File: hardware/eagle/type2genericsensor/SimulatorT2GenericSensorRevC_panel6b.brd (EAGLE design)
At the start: 99.1 x 63.5 mm, 46 parts

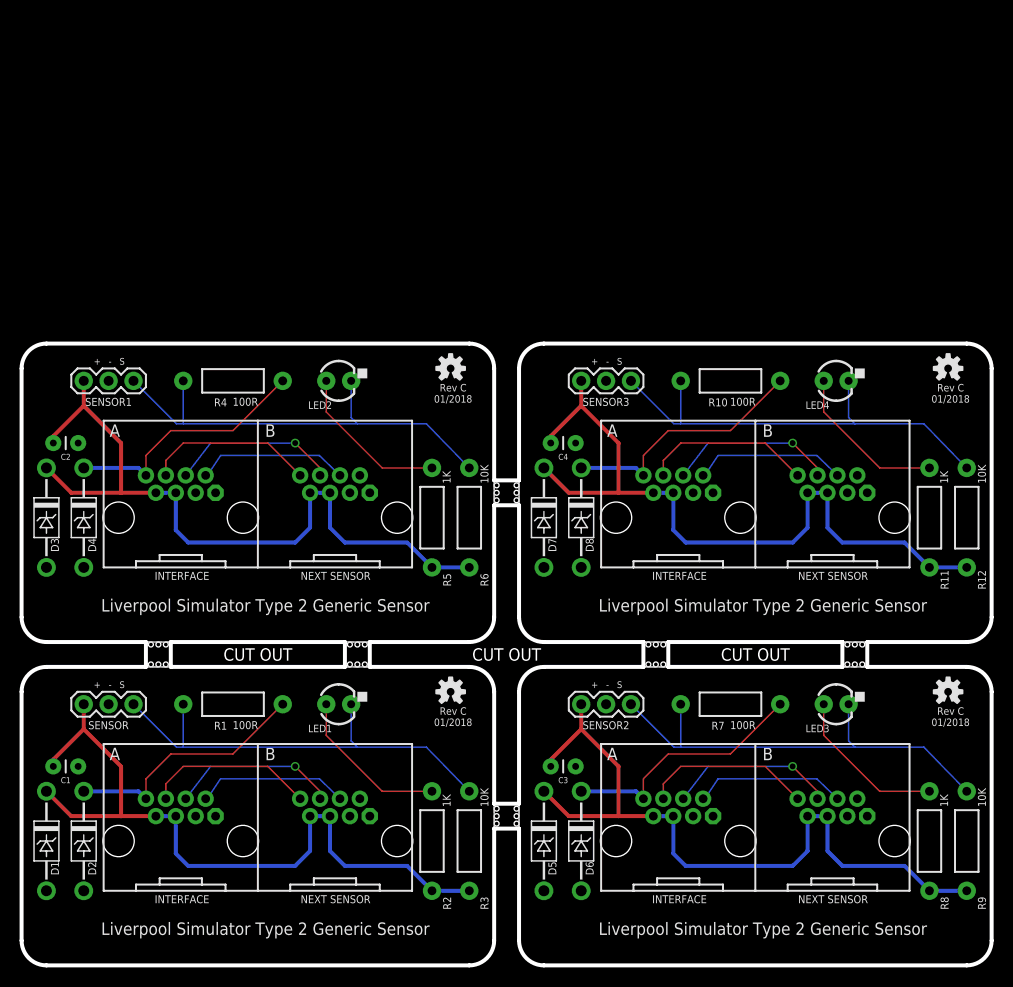
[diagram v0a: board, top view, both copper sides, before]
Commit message: Wider 5mm break-offs
Issues with JLPCB rejecting panelised boards with 2.5mm stamp hole
break-off tabs. Increased tab width to 5mm on all panelised boards.
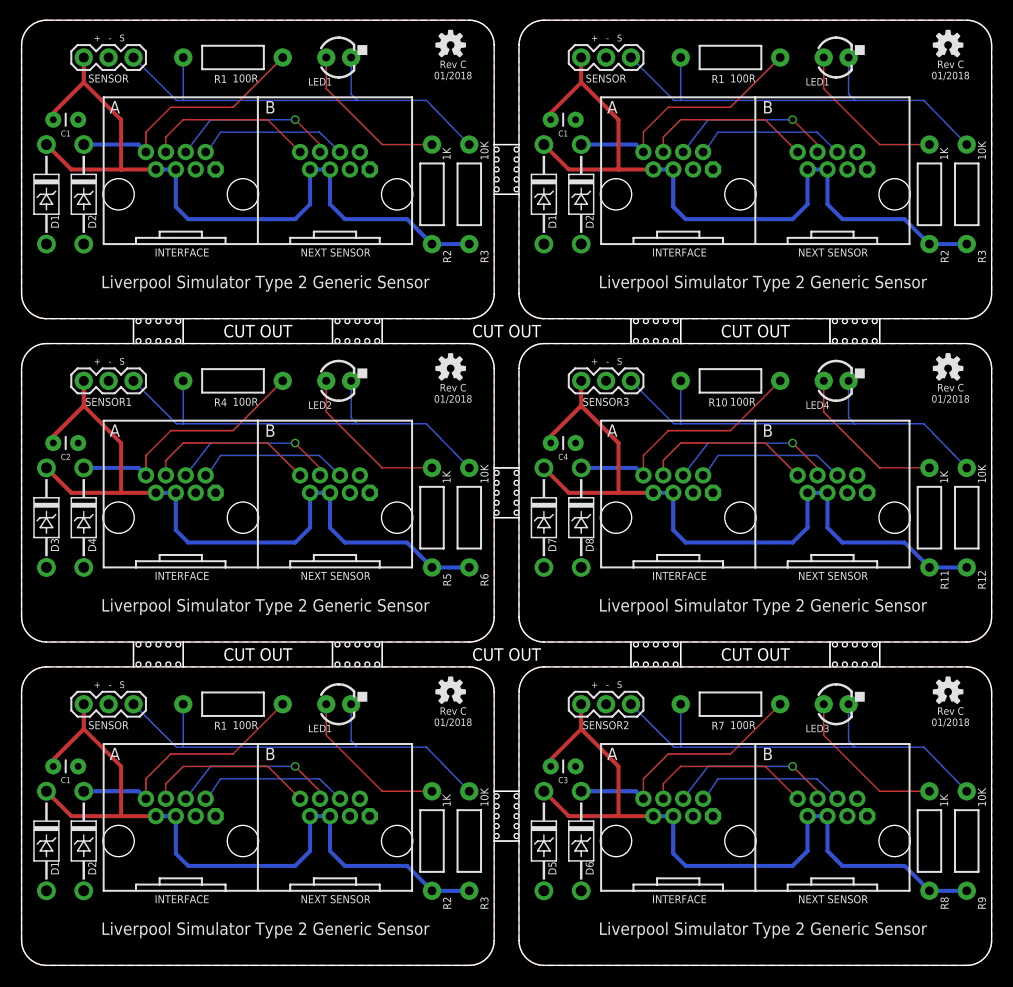
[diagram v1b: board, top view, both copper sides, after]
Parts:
- removed E$2, E$3, E$4, E$5, E$6: (no value), AIC_Custom:STAMP_HOLES
- added C1_1, C1_2: 100nF, SparkFun-Passives:CAP-PTH-SMALL
- added D1_1, D1_2, D2_1, D2_2: SA5.0A, AIC_Custom:DO41_TVS_UNI
- added JP1_1, JP1_2: RJ45-RJHSE-5080-023HOLE, AIC_Custom:RJ45-RJHSE-5080-02-3HOLE
- added LED1_1, LED1_2: Blue, SparkFun-LED:LED3MM
- added LOGO1_1, LOGO1_2: OSHW-LOGOS, SparkFun-Aesthetics:OSHW-LOGO-S
- added R1_1, R1_2: 100R, SparkFun-Passives:AXIAL-0.4
- added R2_1, R2_2: 1K, SparkFun-Passives:AXIAL-0.4
- added R3_1, R3_2: 10K, SparkFun-Passives:AXIAL-0.4
- added SENSOR_1, SENSOR_2: (no value), SparkFun-Connectors:1X03
- E$1: device AIC_Custom:STAMP_HOLES -> AIC_Custom:OUTLINE_PANEL_6_5MM
- moved E$1 46.7 mm to (0.00, 0.00)
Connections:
- new net !OUT!4: D2_1.CATHODE, JP1_1.A8, R1_1.P$1
- new net !OUT!5: D2_2.CATHODE, JP1_2.A8, R1_2.P$1
- new net B21: JP1_1.A6, JP1_1.B8
- new net B22: JP1_2.A6, JP1_2.B8
- new net B31: JP1_1.A4, JP1_1.B6
- new net B32: JP1_2.A4, JP1_2.B6
- new net B41: JP1_1.A2, JP1_1.B4
- new net B42: JP1_2.A2, JP1_2.B4
- new net GND4: C1_1.2, D1_1.ANODE, D2_1.ANODE, JP1_1.A1, JP1_1.A3, JP1_1.B1, JP1_1.B3, SENSOR_1.2
- new net GND5: C1_2.2, D1_2.ANODE, D2_2.ANODE, JP1_2.A1, JP1_2.A3, JP1_2.B1, JP1_2.B3, SENSOR_2.2
- new net LED4: LED1_1.A, R2_1.P$1
- new net LED5: LED1_2.A, R2_2.P$1
- new net SIG4: LED1_1.K, R1_1.P$2, R3_1.P$1, SENSOR_1.3
- new net SIG5: LED1_2.K, R1_2.P$2, R3_2.P$1, SENSOR_2.3
- new net VCC4: C1_1.1, D1_1.CATHODE, JP1_1.A5, JP1_1.A7, JP1_1.B5, JP1_1.B7, R2_1.P$2, R3_1.P$2, SENSOR_1.1
- new net VCC5: C1_2.1, D1_2.CATHODE, JP1_2.A5, JP1_2.A7, JP1_2.B5, JP1_2.B7, R2_2.P$2, R3_2.P$2, SENSOR_2.1
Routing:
- net VCC5: track 0.00 -> 76.1 mm
- net VCC4: track 0.00 -> 76.1 mm
- net SIG5: track 0.00 -> 47.0 mm
- net SIG4: track 0.00 -> 47.0 mm
- net !OUT!4: track 0.00 -> 26.0 mm
- net !OUT!5: track 0.00 -> 26.0 mm
- net B22: track 0.00 -> 17.3 mm
- net B21: track 0.00 -> 17.3 mm
- net B32: track 0.00 -> 17.2 mm, vias 0 -> 1
- net B31: track 0.00 -> 17.2 mm, vias 0 -> 1
- net LED4: track 0.00 -> 16.3 mm
- net LED5: track 0.00 -> 16.3 mm
- net B41: track 0.00 -> 15.6 mm
- net B42: track 0.00 -> 15.6 mm
- added copper zone on layer 1, net GND4
- added copper zone on layer 16, net GND4
- added copper zone on layer 1, net GND5
- added copper zone on layer 16, net GND5
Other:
- board size 99.1 x 63.5 mm -> 99.1 x 96.5 mm
- board text removed: "CUT OUT"
